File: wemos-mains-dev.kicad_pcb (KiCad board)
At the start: 2 copper layers, 74.2 x 46.5 mm, 15 parts, among them J1 Screw_Terminal_01x02, J2 Conn_02x12_Odd_Even, J8 SDA PU, J9 SDA PU, U1 AC-05-3, U2 WeMos_D1_mini

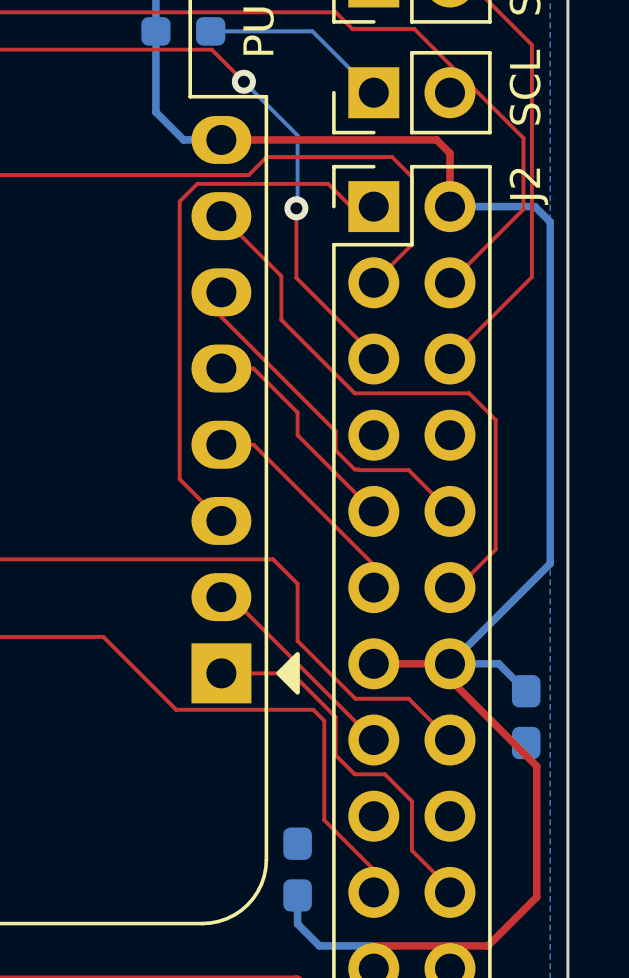
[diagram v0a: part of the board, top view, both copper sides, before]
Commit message: Updated template for KiCAD 7
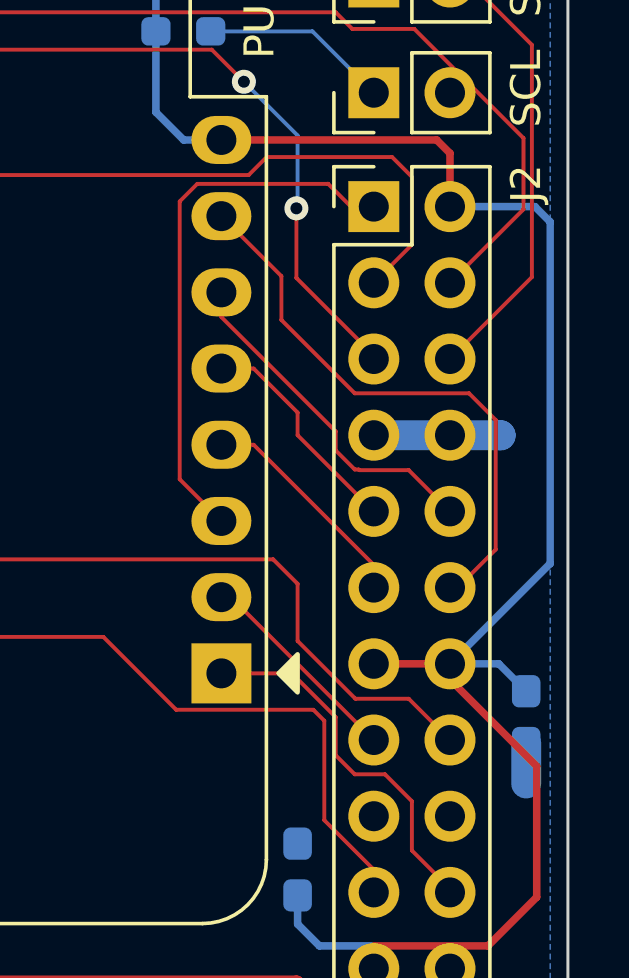
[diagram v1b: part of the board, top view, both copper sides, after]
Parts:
- G***: footprint LOGO -> Chof747 Logos:LOGO large
- H1, H2, H3, H4: footprint MountingHole:MountingHole_3.2mm_M3-smallBorder -> Chof747 Footprints:MountingHole_3.2mm_M3-smallBorder
- U1: footprint Converter_ACDC:AZDelivery AC-05-3 -> Chof747 Footprints:AZDelivery AC-05-3
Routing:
- net GND: track 0.00 -> 5.58 mm
- net +3V3: track 61.5 -> 60.6 mm

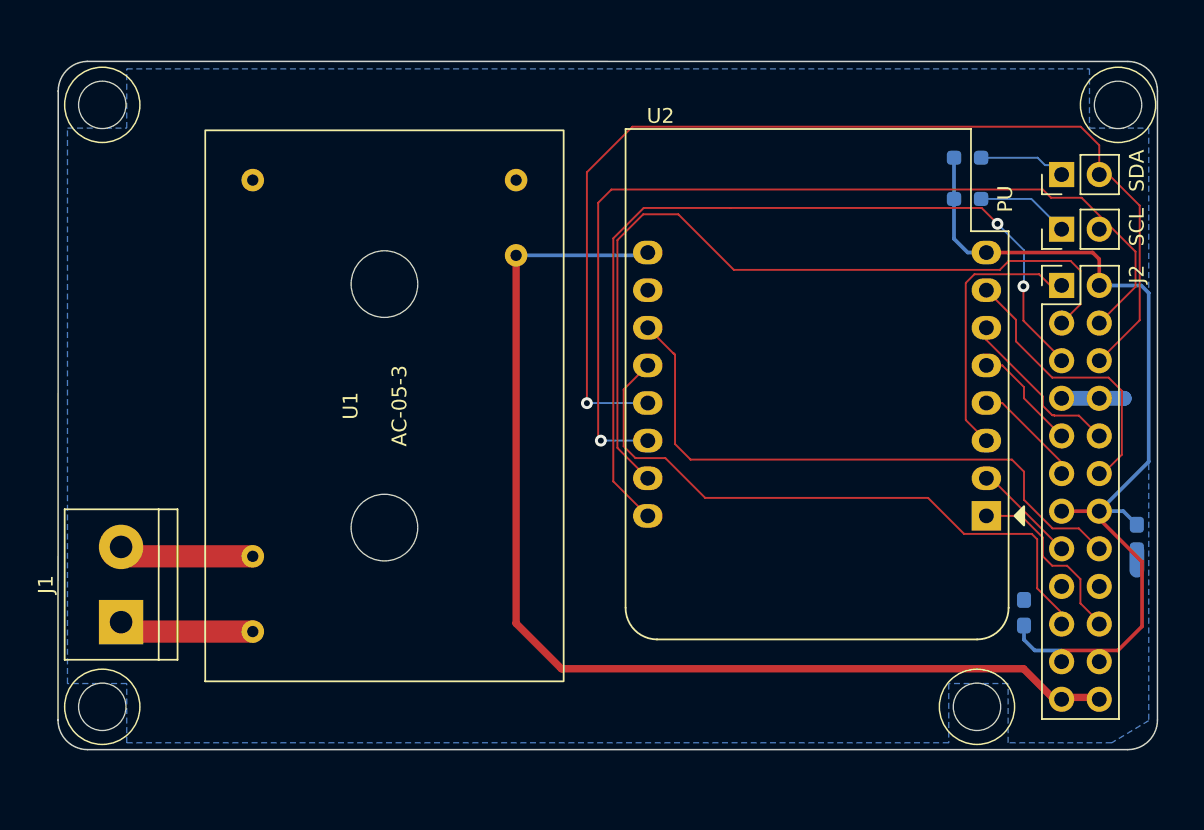
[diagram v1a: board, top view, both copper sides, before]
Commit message: Corrections for rev. 1
- Corrected orientation of power supply footprint
- Reduced ground plane to low voltage side
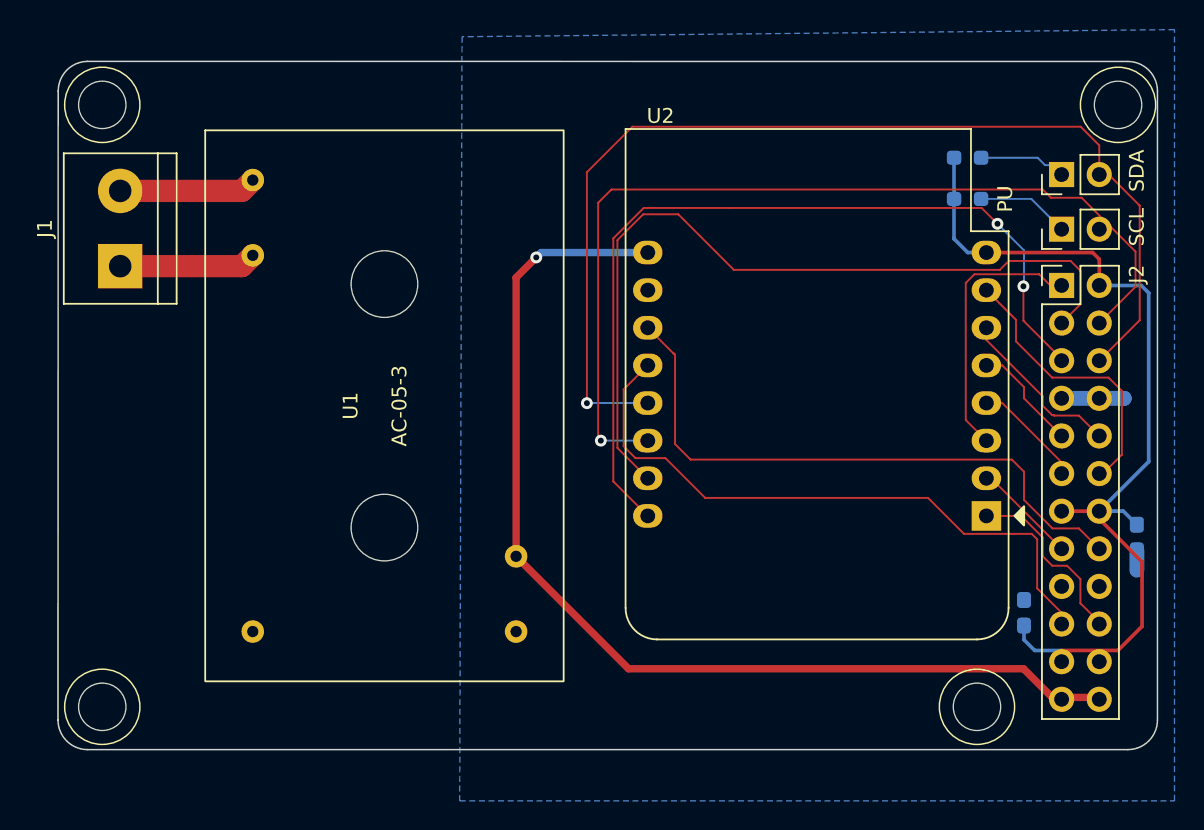
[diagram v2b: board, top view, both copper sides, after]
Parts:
- moved J1 24.0 mm to (71.1, 85.8)
- moved G*** 17.6 mm to (72.4, 104.1)
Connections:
- net +3V3 renamed +3.3V
- J1 pad 1: Net-(J1-Pad1) -> Net-(J1-Pin_1)
- J1 pad 2: Net-(J1-Pad2) -> Net-(J1-Pin_2)
- U1 pad 1: Net-(J1-Pad1) -> Net-(J1-Pin_2)
- U1 pad 2: Net-(J1-Pad2) -> Net-(J1-Pin_1)
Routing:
- net Net-(J1-Pin_2): track 0.00 -> 9.25 mm
- net Net-(J1-Pin_1): track 0.00 -> 9.25 mm
- net Net-(J1-Pad2): track 9.15 -> 0.00 mm
- net Net-(J1-Pad1): track 9.15 -> 0.00 mm
- net +5V: track 75.3 -> 71.8 mm, vias 0 -> 1
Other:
- board text added: "v1.1 (2023)"
- board text removed: "v1.0 (2023)"
